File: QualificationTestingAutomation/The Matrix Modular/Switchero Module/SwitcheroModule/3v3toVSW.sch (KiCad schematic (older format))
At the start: 6 parts, among them Q3 2N7002DW

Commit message: Cleaned up the libraries Cleaned up the tracks Adjusted footprints to the manufacturers minimum size.
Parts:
- C3: symbol TheMatrix-rescue:CAP-passive-SchematicAutomation-rescue -> SwitcheroModule-rescue:CAP-passive-SchematicAutomation-rescue-TheMatrix-rescue
- Q3: symbol TheMatrix-rescue:2N7002DW-dk_Transistors-FETs-MOSFETs-Arrays-SchematicAutomation-rescue -> SwitcheroModule-rescue:2N7002DW-dk_Transistors-FETs-MOSFETs-Arrays-SchematicAutomation-rescue-TheMatrix-rescue
- R13, R14, R15, R16: symbol TheMatrix-rescue:RESISTOR-passive-SchematicAutomation-rescue -> SwitcheroModule-rescue:RESISTOR-passive-SchematicAutomation-rescue-TheMatrix-rescue
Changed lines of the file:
@@
 Tx_3V3
 $Comp
-L TheMatrix-rescue:2N7002DW-dk_Transistors-FETs-MOSFETs-Arrays-SchematicAutomation-rescue Q?
+L SwitcheroModule-rescue:2N7002DW-dk_Transistors-FETs-MOSFETs-Arrays-SchematicAutomation-rescue-TheMatrix-rescue Q?
 U 1 1 5CA21D7D
 P 3300 3350
@@
 AR Path="/5C90F514/5CA214F0/5CA2401F/5CA21D7D" Ref="Q5"  Part="1"
 AR Path="/5C90F514/5CA214F0/5CA2417E/5CA21D7D" Ref="Q7"  Part="1"
+AR Path="/5CA21D7D" Ref="Q7"  Part="1"
 F 0 "Q7" H 3300 3837 60  0000 C CNN
 F 1 "2N7002DW" H 3300 3731 60  0000 C CNN
@@
 	3600 3150 3800 3150
 $Comp
-L TheMatrix-rescue:RESISTOR-passive-SchematicAutomation-rescue R?
+L SwitcheroModule-rescue:RESISTOR-passive-SchematicAutomation-rescue-TheMatrix-rescue R?
 U 1 1 5CA21D87
 P 4050 3150
@@
 Connection ~ 2700 3750
 $Comp
-L TheMatrix-rescue:RESISTOR-passive-SchematicAutomation-rescue R?
+L SwitcheroModule-rescue:RESISTOR-passive-SchematicAutomation-rescue-TheMatrix-rescue R?
 U 1 1 5CA21D95
 P 2250 3750
@@
 	2000 3700 2000 3750
 $Comp
-L TheMatrix-rescue:RESISTOR-passive-SchematicAutomation-rescue R?
+L SwitcheroModule-rescue:RESISTOR-passive-SchematicAutomation-rescue-TheMatrix-rescue R?
 U 1 1 5CA21DAB
 P 4450 3300
@@
 	4650 3450 4450 3450
 $Comp
-L TheMatrix-rescue:RESISTOR-passive-SchematicAutomation-rescue R?
+L SwitcheroModule-rescue:RESISTOR-passive-SchematicAutomation-rescue-TheMatrix-rescue R?
 U 1 1 5CA21DB6
 P 4450 3600
@@
 	4450 3700 4450 3750
 $Comp
-L TheMatrix-rescue:CAP-passive-SchematicAutomation-rescue C?
+L SwitcheroModule-rescue:CAP-passive-SchematicAutomation-rescue-TheMatrix-rescue C?
 U 1 1 5CA21DC3
 P 4750 3450

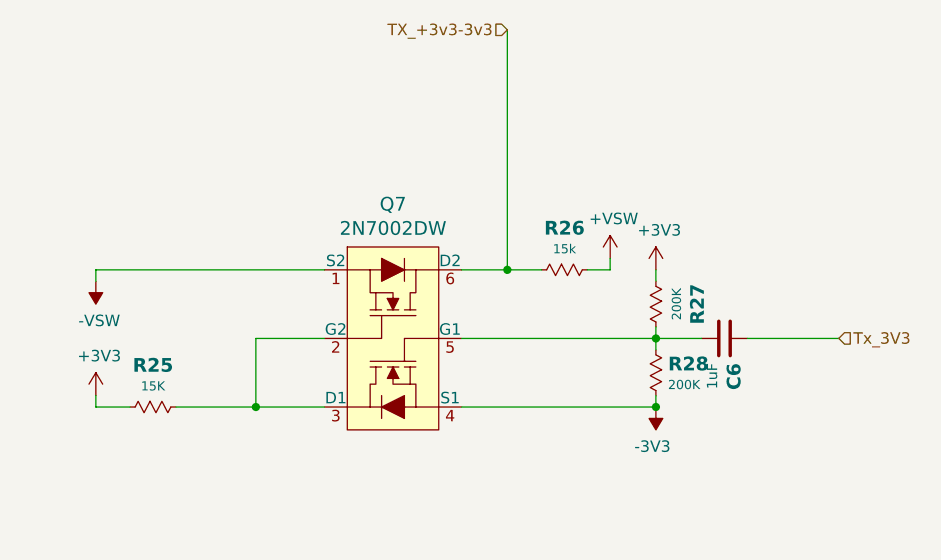
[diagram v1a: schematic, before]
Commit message: Added Voltage and current measurment of the muxes and relays to the MSP Some clean up of the tracks.
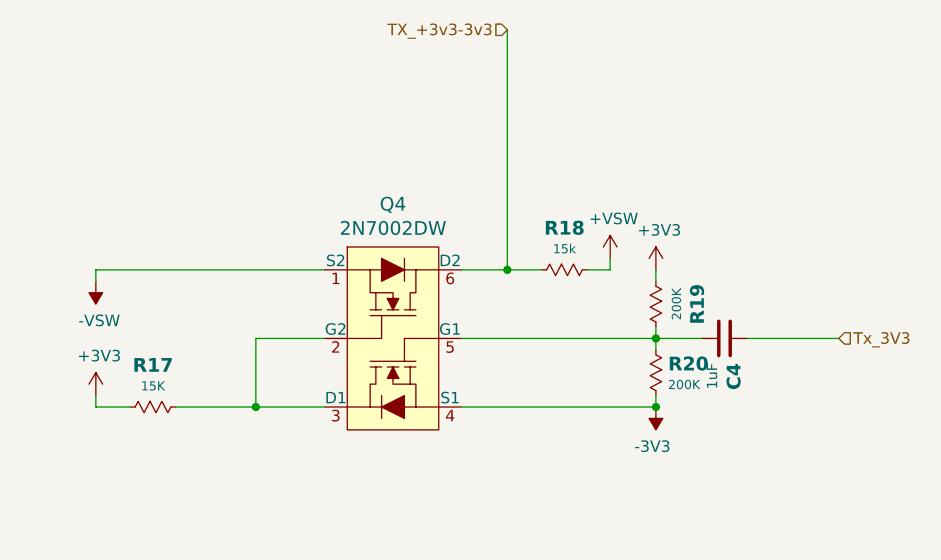
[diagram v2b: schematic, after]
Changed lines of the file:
@@
 EESchema Schematic File Version 4
 LIBS:SwitcheroModule-cache
-EELAYER 26 0
+EELAYER 29 0
 EELAYER END
 $Descr A4 11693 8268
@@
 AR Path="/5C90F514/5CA214F0/5CA2417E/5CA21D7D" Ref="Q7"  Part="1"
 AR Path="/5CA21D7D" Ref="Q7"  Part="1"
-F 0 "Q7" H 3300 3837 60  0000 C CNN
+F 0 "Q4" H 3300 3837 60  0000 C CNN
 F 1 "2N7002DW" H 3300 3731 60  0000 C CNN
 F 2 "digikey-footprints:SOT-363" H 3500 3550 60  0001 L CNN
@@
 AR Path="/5C90F514/5CA214F0/5CA2401F/5CA21D87" Ref="R22"  Part="1"
 AR Path="/5C90F514/5CA214F0/5CA2417E/5CA21D87" Ref="R26"  Part="1"
-F 0 "R26" H 4050 3332 60  0000 C CNB
+F 0 "R18" H 4050 3332 60  0000 C CNB
 F 1 "15k" H 4050 3241 40  0000 C CNN
 F 2 "Resistor_SMD:R_0402_1005Metric" H 4050 3010 40  0001 C CNN
@@
 AR Path="/5C90F514/5CA214F0/5CA2401F/5CA21D95" Ref="R21"  Part="1"
 AR Path="/5C90F514/5CA214F0/5CA2417E/5CA21D95" Ref="R25"  Part="1"
-F 0 "R25" H 2250 3932 60  0000 C CNB
+F 0 "R17" H 2250 3932 60  0000 C CNB
 F 1 "15K" H 2250 3841 40  0000 C CNN
 F 2 "Resistor_SMD:R_0402_1005Metric" H 2250 3610 40  0001 C CNN
@@
 AR Path="/5C90F514/5CA214F0/5CA2401F/5CA21DA1" Ref="#PWR0151"  Part="1"
 AR Path="/5C90F514/5CA214F0/5CA2417E/5CA21DA1" Ref="#PWR0156"  Part="1"
-F 0 "#PWR0156" H 2000 3300 50  0001 C CNN
+F 0 "#PWR0146" H 2000 3300 50  0001 C CNN
 F 1 "-VSW" H 2015 3373 50  0000 C CNN
 F 2 "" H 2000 3200 50  0001 C CNN
@@
 AR Path="/5C90F514/5CA214F0/5CA2401F/5CA21DAB" Ref="R23"  Part="1"
 AR Path="/5C90F514/5CA214F0/5CA2417E/5CA21DAB" Ref="R27"  Part="1"
-F 0 "R27" H 4450 3482 60  0000 C CNB
+F 0 "R19" H 4450 3482 60  0000 C CNB
 F 1 "200K" H 4450 3391 40  0000 C CNN
 F 2 "Resistor_SMD:R_0402_1005Metric" H 4450 3160 40  0001 C CNN
@@
 AR Path="/5C90F514/5CA214F0/5CA2401F/5CA21DB6" Ref="R24"  Part="1"
 AR Path="/5C90F514/5CA214F0/5CA2417E/5CA21DB6" Ref="R28"  Part="1"
-F 0 "R28" V 4412 3653 60  0000 L CNB
+F 0 "R20" V 4412 3653 60  0000 L CNB
 F 1 "200K" V 4503 3653 40  0000 L CNN
 F 2 "Resistor_SMD:R_0402_1005Metric" H 4450 3460 40  0001 C CNN
@@
 AR Path="/5C90F514/5CA214F0/5CA2401F/5CA21DC3" Ref="C5"  Part="1"
 AR Path="/5C90F514/5CA214F0/5CA2417E/5CA21DC3" Ref="C6"  Part="1"
-F 0 "C6" H 4858 3492 60  0000 L CNB
+F 0 "C4" H 4858 3492 60  0000 L CNB
 F 1 "1uF" H 4858 3397 45  0000 L CNN
 F 2 "Capacitor_SMD:C_0603_1608Metric_Pad1.05x0.95mm_HandSolder" H 4785 3295 40  0001 L CNN
@@
 AR Path="/5C90F514/5CA214F0/5CA2401F/5CA21DCC" Ref="#PWR0152"  Part="1"
 AR Path="/5C90F514/5CA214F0/5CA2417E/5CA21DCC" Ref="#PWR0160"  Part="1"
-F 0 "#PWR0160" H 4450 3000 50  0001 C CNN
+F 0 "#PWR0147" H 4450 3000 50  0001 C CNN
 F 1 "+3V3" H 4465 3323 50  0000 C CNN
 F 2 "" H 4450 3150 50  0001 C CNN
@@
 AR Path="/5C90F514/5CA214F0/5CA2401F/5CA21DD2" Ref="#PWR0153"  Part="1"
 AR Path="/5C90F514/5CA214F0/5CA2417E/5CA21DD2" Ref="#PWR0162"  Part="1"
-F 0 "#PWR0162" H 2000 3550 50  0001 C CNN
+F 0 "#PWR0148" H 2000 3550 50  0001 C CNN
 F 1 "+3V3" H 2015 3873 50  0000 C CNN
 F 2 "" H 2000 3700 50  0001 C CNN
@@
 AR Path="/5C90F514/5CA214F0/5CA2401F/5CA21DD8" Ref="#PWR0154"  Part="1"
 AR Path="/5C90F514/5CA214F0/5CA2417E/5CA21DD8" Ref="#PWR0163"  Part="1"
-F 0 "#PWR0163" H 4450 3850 50  0001 C CNN
+F 0 "#PWR0149" H 4450 3850 50  0001 C CNN
 F 1 "-3V3" H 4465 3923 50  0000 C CNN
 F 2 "" H 4450 3750 50  0001 C CNN
@@
 AR Path="/5C90F514/5CA214F0/5CA2401F/5CA21DDF" Ref="#PWR0155"  Part="1"
 AR Path="/5C90F514/5CA214F0/5CA2417E/5CA21DDF" Ref="#PWR0166"  Part="1"
-F 0 "#PWR0166" H 4250 2950 50  0001 C CNN
+F 0 "#PWR0150" H 4250 2950 50  0001 C CNN
 F 1 "+VSW" H 4265 3273 50  0000 C CNN
 F 2 "" H 4250 3100 50  0001 C CNN

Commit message: Schematic Clean ups the layout needs to be changed
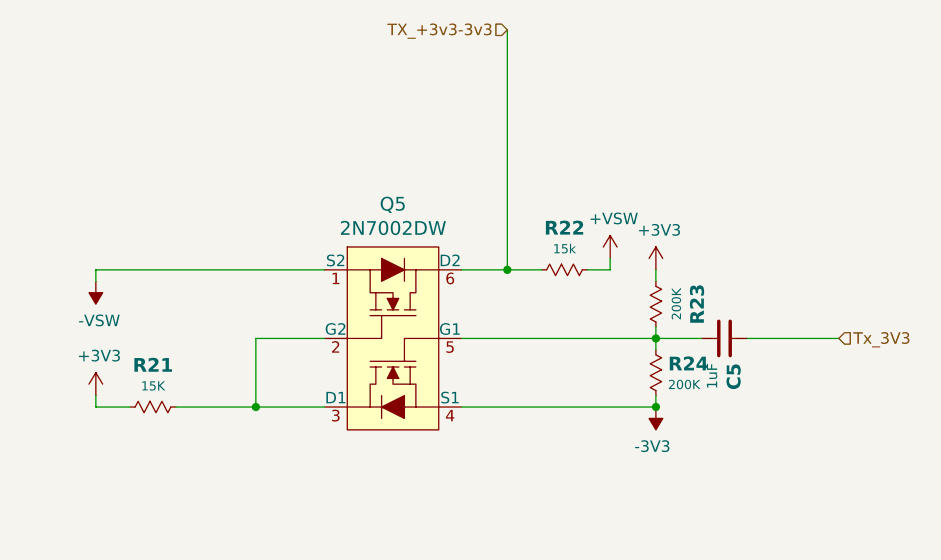
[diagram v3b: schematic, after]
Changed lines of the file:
@@
 AR Path="/5C90F514/5CA214F0/5CA2417E/5CA21D7D" Ref="Q7"  Part="1"
 AR Path="/5CA21D7D" Ref="Q7"  Part="1"
-F 0 "Q4" H 3300 3837 60  0000 C CNN
+F 0 "Q5" H 3300 3837 60  0000 C CNN
 F 1 "2N7002DW" H 3300 3731 60  0000 C CNN
 F 2 "digikey-footprints:SOT-363" H 3500 3550 60  0001 L CNN
@@
 AR Path="/5C90F514/5CA214F0/5CA2401F/5CA21D87" Ref="R22"  Part="1"
 AR Path="/5C90F514/5CA214F0/5CA2417E/5CA21D87" Ref="R26"  Part="1"
-F 0 "R18" H 4050 3332 60  0000 C CNB
+F 0 "R22" H 4050 3332 60  0000 C CNB
 F 1 "15k" H 4050 3241 40  0000 C CNN
 F 2 "Resistor_SMD:R_0402_1005Metric" H 4050 3010 40  0001 C CNN
@@
 AR Path="/5C90F514/5CA214F0/5CA2401F/5CA21D95" Ref="R21"  Part="1"
 AR Path="/5C90F514/5CA214F0/5CA2417E/5CA21D95" Ref="R25"  Part="1"
-F 0 "R17" H 2250 3932 60  0000 C CNB
+F 0 "R21" H 2250 3932 60  0000 C CNB
 F 1 "15K" H 2250 3841 40  0000 C CNN
 F 2 "Resistor_SMD:R_0402_1005Metric" H 2250 3610 40  0001 C CNN
@@
 AR Path="/5C90F514/5CA214F0/5CA2401F/5CA21DA1" Ref="#PWR0151"  Part="1"
 AR Path="/5C90F514/5CA214F0/5CA2417E/5CA21DA1" Ref="#PWR0156"  Part="1"
-F 0 "#PWR0146" H 2000 3300 50  0001 C CNN
+F 0 "#PWR0156" H 2000 3300 50  0001 C CNN
 F 1 "-VSW" H 2015 3373 50  0000 C CNN
 F 2 "" H 2000 3200 50  0001 C CNN
@@
 AR Path="/5C90F514/5CA214F0/5CA2401F/5CA21DAB" Ref="R23"  Part="1"
 AR Path="/5C90F514/5CA214F0/5CA2417E/5CA21DAB" Ref="R27"  Part="1"
-F 0 "R19" H 4450 3482 60  0000 C CNB
+F 0 "R23" H 4450 3482 60  0000 C CNB
 F 1 "200K" H 4450 3391 40  0000 C CNN
 F 2 "Resistor_SMD:R_0402_1005Metric" H 4450 3160 40  0001 C CNN
@@
 AR Path="/5C90F514/5CA214F0/5CA2401F/5CA21DB6" Ref="R24"  Part="1"
 AR Path="/5C90F514/5CA214F0/5CA2417E/5CA21DB6" Ref="R28"  Part="1"
-F 0 "R20" V 4412 3653 60  0000 L CNB
+F 0 "R24" V 4412 3653 60  0000 L CNB
 F 1 "200K" V 4503 3653 40  0000 L CNN
 F 2 "Resistor_SMD:R_0402_1005Metric" H 4450 3460 40  0001 C CNN
@@
 AR Path="/5C90F514/5CA214F0/5CA2401F/5CA21DC3" Ref="C5"  Part="1"
 AR Path="/5C90F514/5CA214F0/5CA2417E/5CA21DC3" Ref="C6"  Part="1"
-F 0 "C4" H 4858 3492 60  0000 L CNB
+F 0 "C5" H 4858 3492 60  0000 L CNB
 F 1 "1uF" H 4858 3397 45  0000 L CNN
 F 2 "Capacitor_SMD:C_0603_1608Metric_Pad1.05x0.95mm_HandSolder" H 4785 3295 40  0001 L CNN
@@
 AR Path="/5C90F514/5CA214F0/5CA2401F/5CA21DCC" Ref="#PWR0152"  Part="1"
 AR Path="/5C90F514/5CA214F0/5CA2417E/5CA21DCC" Ref="#PWR0160"  Part="1"
-F 0 "#PWR0147" H 4450 3000 50  0001 C CNN
+F 0 "#PWR0160" H 4450 3000 50  0001 C CNN
 F 1 "+3V3" H 4465 3323 50  0000 C CNN
 F 2 "" H 4450 3150 50  0001 C CNN
@@
 AR Path="/5C90F514/5CA214F0/5CA2401F/5CA21DD2" Ref="#PWR0153"  Part="1"
 AR Path="/5C90F514/5CA214F0/5CA2417E/5CA21DD2" Ref="#PWR0162"  Part="1"
-F 0 "#PWR0148" H 2000 3550 50  0001 C CNN
+F 0 "#PWR0162" H 2000 3550 50  0001 C CNN
 F 1 "+3V3" H 2015 3873 50  0000 C CNN
 F 2 "" H 2000 3700 50  0001 C CNN
@@
 AR Path="/5C90F514/5CA214F0/5CA2401F/5CA21DD8" Ref="#PWR0154"  Part="1"
 AR Path="/5C90F514/5CA214F0/5CA2417E/5CA21DD8" Ref="#PWR0163"  Part="1"
-F 0 "#PWR0149" H 4450 3850 50  0001 C CNN
+F 0 "#PWR0163" H 4450 3850 50  0001 C CNN
 F 1 "-3V3" H 4465 3923 50  0000 C CNN
 F 2 "" H 4450 3750 50  0001 C CNN
@@
 AR Path="/5C90F514/5CA214F0/5CA2401F/5CA21DDF" Ref="#PWR0155"  Part="1"
 AR Path="/5C90F514/5CA214F0/5CA2417E/5CA21DDF" Ref="#PWR0166"  Part="1"
-F 0 "#PWR0150" H 4250 2950 50  0001 C CNN
+F 0 "#PWR0166" H 4250 2950 50  0001 C CNN
 F 1 "+VSW" H 4265 3273 50  0000 C CNN
 F 2 "" H 4250 3100 50  0001 C CNN
